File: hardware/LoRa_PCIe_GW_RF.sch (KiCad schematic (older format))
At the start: 94 parts, among them U700 NC, U800 SX1250, U801 SAW Filter, U802 SKY66423-11, U803 SAW Filter, U805 SAW Filter, U900 SX1250, Y800 TCXO

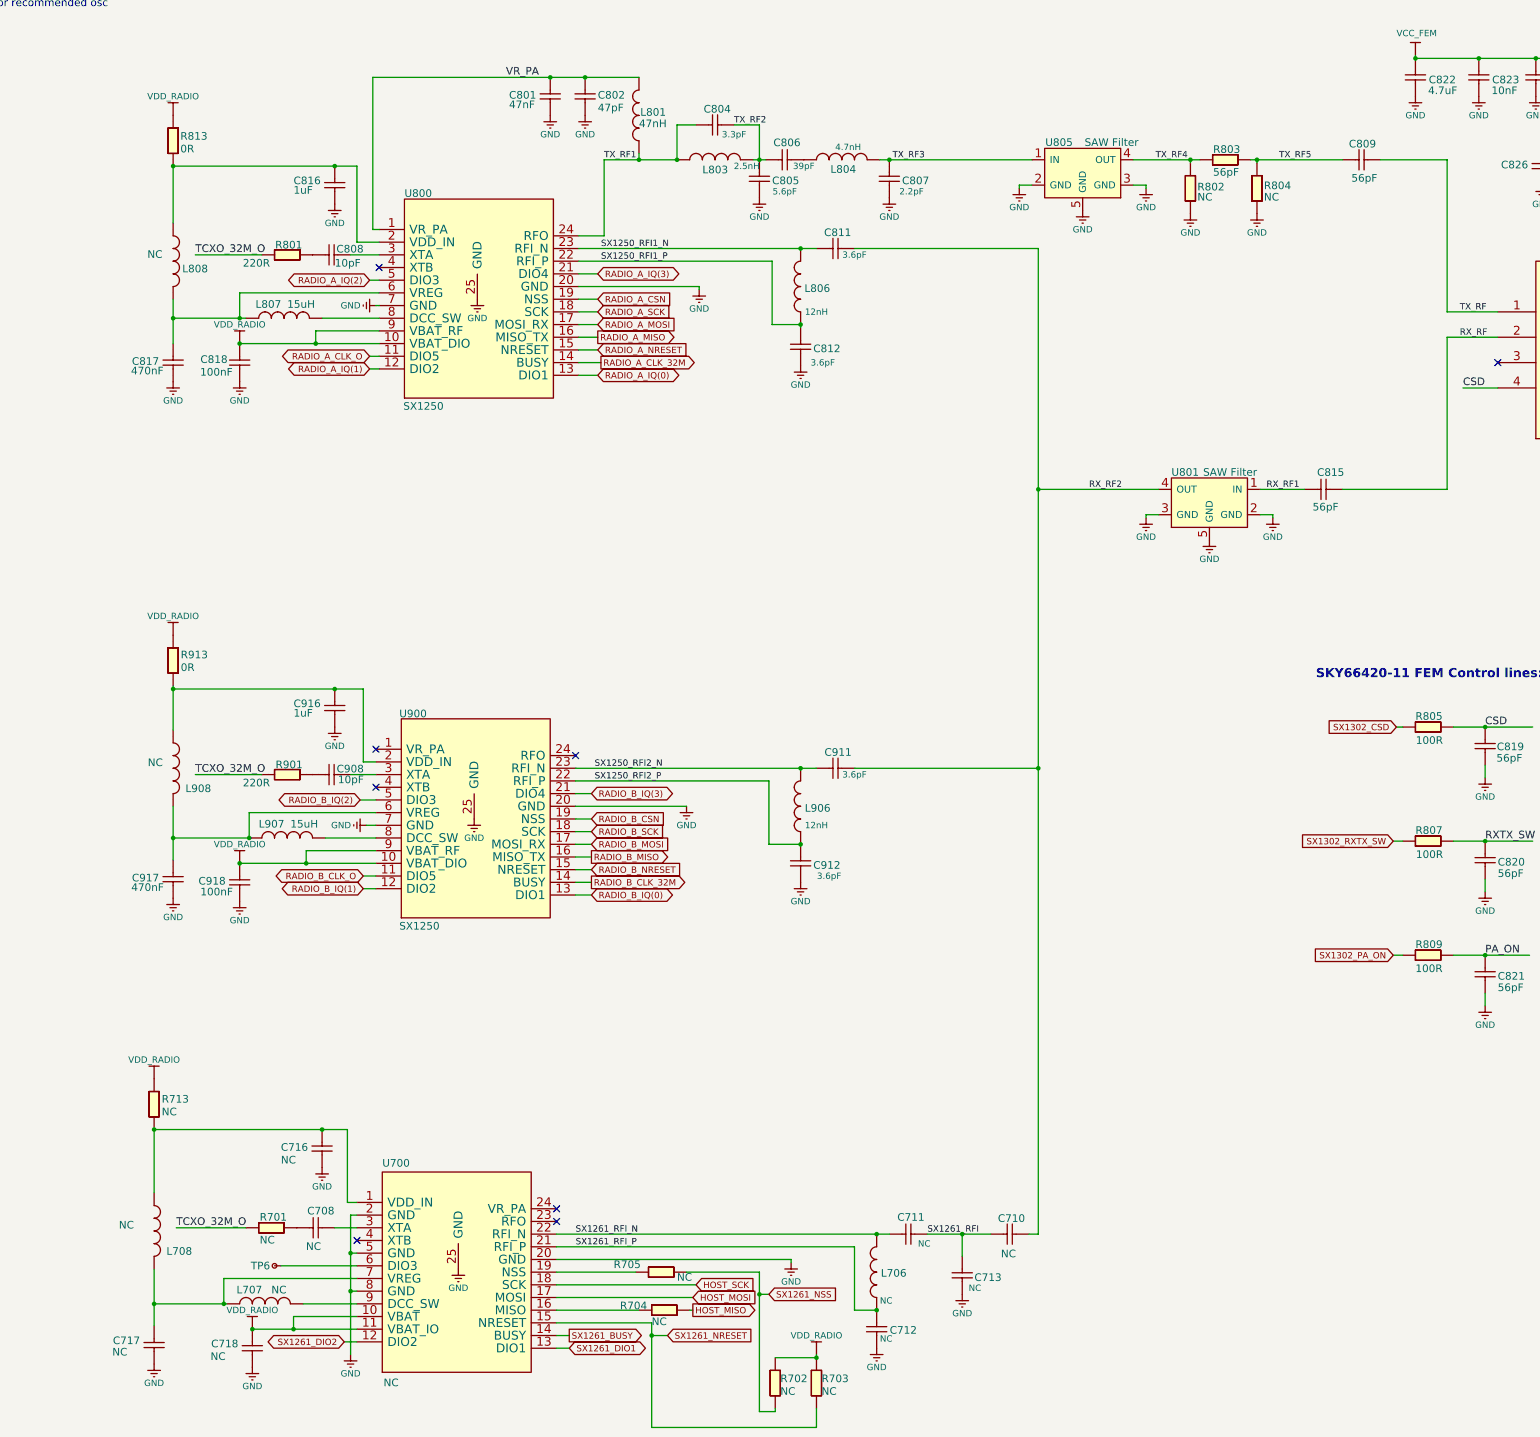
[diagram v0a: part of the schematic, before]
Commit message: Updates according to Corecell_V3 Reference design.
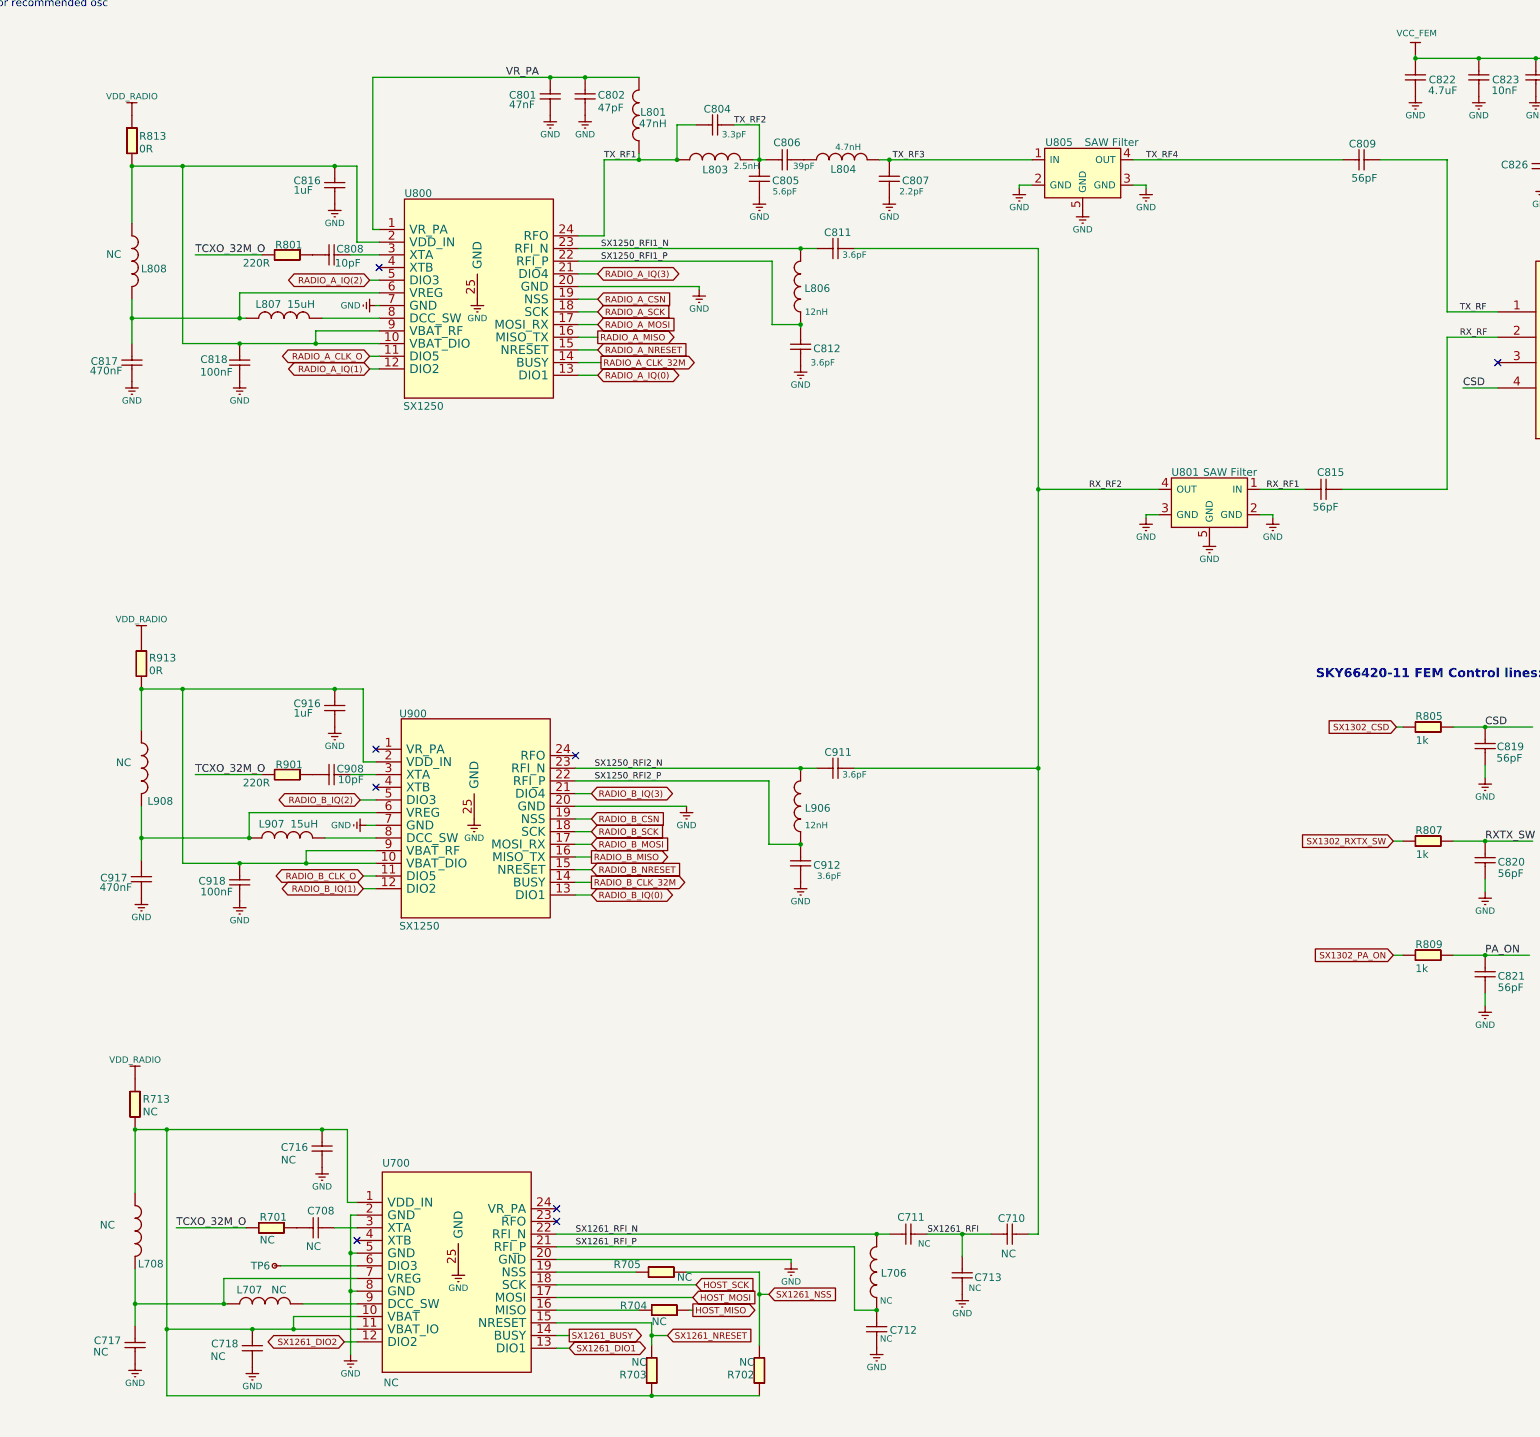
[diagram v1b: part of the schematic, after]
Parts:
- removed R802, R804: NC, LoRa_PCIe_GW:rlc_201_smd_small, symbol LoRa_PCIe_GW-rescue:Resistor-
- removed R803: 56pF, LoRa_PCIe_GW:ccer_201_smd_small, symbol LoRa_PCIe_GW-rescue:Resistor-
- C718, C818, C918: footprint LoRa_PCIe_GW:ccer_201_smd_small -> LoRa_PCIe_GW:ccer_402_smd_small; Description 0.1µF ±10% 16V Ceramic Capacitor X7S 0201 (0603 Metric) -> Multilayer ceramic capacitors X7R ±10%, 16V; Part Number GRM033C71C104KE14D -> GMD155R71C104KA11; Supplier Link https://www.digikey.com/en/products/detail/murata-electronics/GRM033C71C104KE14D/5027472 -> https://www.digikey.com/en/products/detail/murata-electronics/GMD155R71C104KA11D/10696609
- R805, R807, R809: value 100R -> 1k; Description 100 Ohms ±1% 0.05W, 1/20W Chip Resistor 0201 (0603 Metric) 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 -> 1k Ohm ±5% 0.05W, 1/20W Chip Resistor 0201 (0603 Metric) - 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; Part Number CRCW0201100R -> CRCW02011K00JNED; Price[1k] 0.037 -> 0.073; Supplier Link https://www.digikey.com/en/products/detail/vishay-dale/CRCW0201100RFKED/1967973 -> https://www.digikey.com/en/products/detail/vishay-dale/CRCW02011K00JNED/1178450
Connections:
- net TX_RF5 is gone; now on net TX_RF4: C809.1
- net VDD_RADIO: no longer C718.2, C818.2, C918.2, R702.1, R703.1, U700.10 (VBAT), U700.11 (VBAT_IO), U800.10 (VBAT_DIO), U800.9 (VBAT_RF), U900.10 (VBAT_DIO), U900.9 (VBAT_RF)
- net at C716.2, L708.2, R713.2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: now also C718.2, R702.1, R703.1, U700.10 (VBAT), U700.11 (VBAT_IO)
- net at C816.2, L808.2, R813.2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: now also C818.2, U800.10 (VBAT_DIO), U800.9 (VBAT_RF)
- net at C916.2, L908.2, R913.2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: now also C918.2, U900.10 (VBAT_DIO), U900.9 (VBAT_RF)
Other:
- moved on the sheet: C717, C817, C917, L708, L808, L908, R702, R703, R713, R813, R913

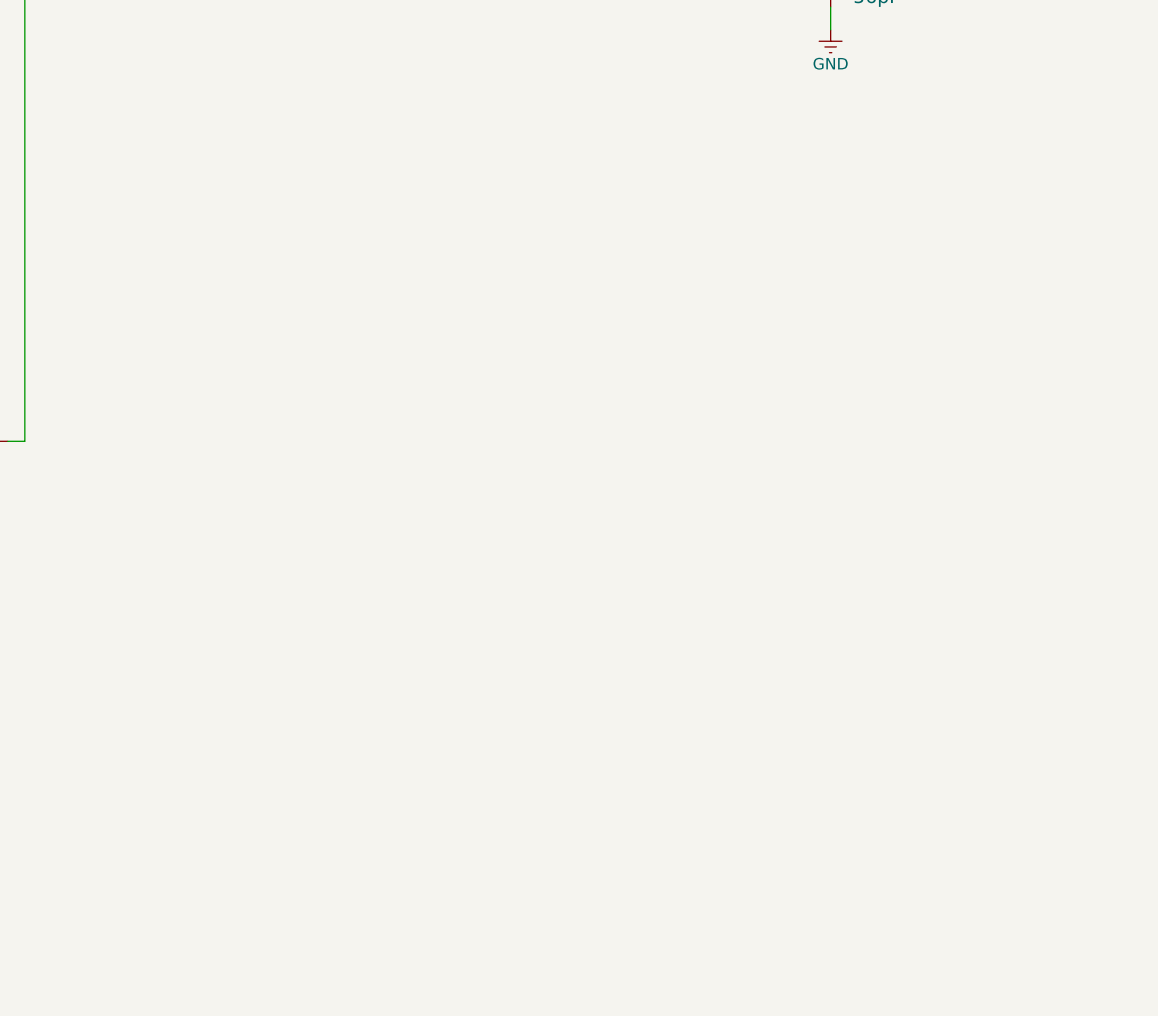
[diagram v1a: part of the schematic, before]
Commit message: Added BOM for non GNSS variants. Few part numbers corrected in design.
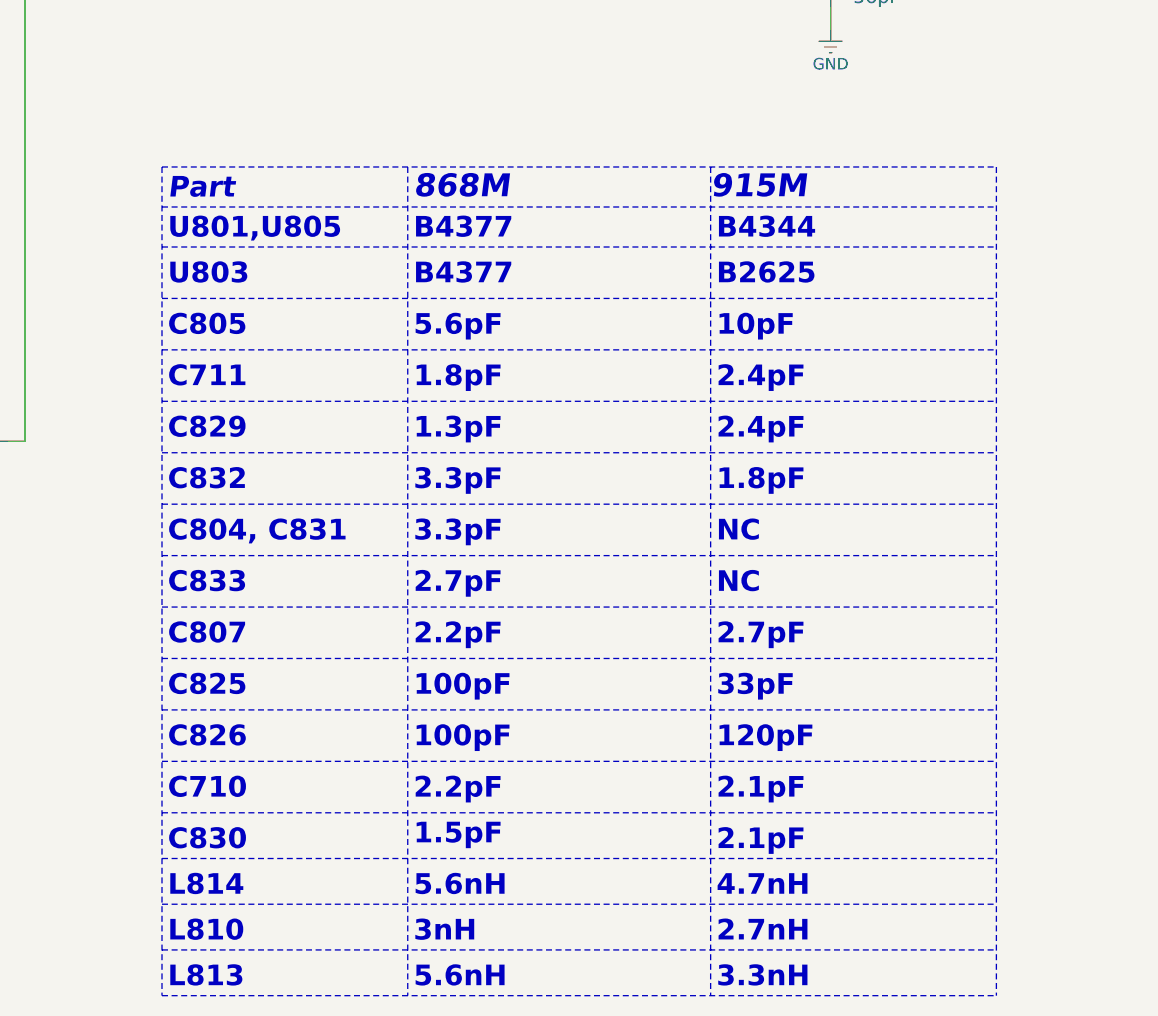
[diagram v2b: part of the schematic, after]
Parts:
- C833: Description 2.7pF ±0.25pF 25V Ceramic Capacitor C0G, NP0 0201 (0603 Met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 -> 2.7 pF ±0.1pF 50V Ceramic Capacitor C0G, NP0 0201 (0603 Met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; Part Number GJM0335C1E2R7CB01J -> GJM0335C1H2R7BB01D; Supplier Link https://www.digikey.com/en/products/detail/murata-electronics/GJM0335C1E2R7CB01J/2592574 -> https://www.digikey.com/en/products/detail/murata-electronics/GJM0335C1H2R7BB01D/9758987
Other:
- note added: "1.3pF"
- note added: "1.5pF"
- note added: "1.8pF"
- note added: "100pF"
- note added: "10pF"
- note added: "120pF"
- note added: "2.1pF"
- note added: "2.2pF"
- note added: "2.4pF"
- note added: "2.7nH"
- note added: "2.7pF"
- note added: "3.3nH"
- note added: "3.3pF"
- note added: "33pF"
- note added: "3nH"
- note added: "4.7nH"
- note added: "5.6nH"
- note added: "5.6pF"
- note added: "868M"
- note added: "915M"
- note added: "B2625"
- note added: "B4344"
- note added: "B4377"
- note added: "C710"
- note added: "C711"
- note added: "C804, C831"
- note added: "C805"
- note added: "C807"
- note added: "C825"
- note added: "C826"
- note added: "C829"
- note added: "C830"
- note added: "C832"
- note added: "C833"
- note added: "L810"
- note added: "L813"
- note added: "L814"
- note added: "NC"
- note added: "Part"
- note added: "U801,U805"
- note added: "U803"
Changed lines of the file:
@@
 F 2 "LoRa_PCIe_GW:ccer_201_smd_small" H 19500 6775 50  0001 C CNN
 F 3 "" H 19500 6775 50  0001 C CNN
-F 4 "2.7pF ±0.25pF 25V Ceramic Capacitor C0G, NP0 0201 (0603 Metric)" H 19500 6775 50  0001 C CNN "Description"
+F 4 "2.7 pF ±0.1pF 50V Ceramic Capacitor C0G, NP0 0201 (0603 Metric)" H 19500 6775 50  0001 C CNN "Description"
 F 5 "Murata" H 19500 6775 50  0001 C CNN "Manufacturer"
-F 6 "GJM0335C1E2R7CB01J" H 19500 6775 50  0001 C CNN "Part Number"
+F 6 "GJM0335C1H2R7BB01D" H 19500 6775 50  0001 C CNN "Part Number"
 F 7 "0.008" H 19500 6775 50  0001 C CNN "Price[1k]"
-F 8 "https://www.digikey.com/en/products/detail/murata-electronics/GJM0335C1E2R7CB01J/2592574" H 19500 6775 50  0001 C CNN "Supplier Link"
+F 8 "https://www.digikey.com/en/products/detail/murata-electronics/GJM0335C1H2R7BB01D/9758987" H 19500 6775 50  0001 C CNN "Supplier Link"
 	1    19500 6775
 	0    1    1    0
@@
 	8800 14550 4975 14550
 Connection ~ 4975 14025
+Wire Notes Line
+	12450 15100 16100 15100
+Wire Notes Line style solid rgb(0, 0, 0)
+	12450 12075 16100 12075
+Wire Notes Line style solid rgb(0, 0, 0)
+	12450 12250 16100 12250
+Wire Notes Line rgb(0, 0, 0)
+	12450 12425 16100 12425
+Text Notes 12475 12225 0    90   Italic 18
+Part
+Text Notes 13550 12225 0    100  Italic 20
+868M
+Text Notes 14850 12225 0    100  Italic 20
+915M
+Text Notes 12475 12400 0    90   ~ 18
+U801,U805
+Text Notes 13550 12400 0    90   ~ 18
+B4377
+Text Notes 14875 12400 0    90   ~ 18
+B4344
+Wire Notes Line
+	12450 12650 16100 12650
+Wire Notes Line
+	12450 12875 16100 12875
+Wire Notes Line
+	12450 13100 16100 13100
+Wire Notes Line
+	12450 13325 16100 13325
+Wire Notes Line
+	12450 13550 16100 13550
+Text Notes 12475 12600 0    90   ~ 18
+U803
+Text Notes 13550 12600 0    90   ~ 18
+B4377
+Text Notes 14875 12600 0    90   ~ 18
+B2625
+Text Notes 12475 12825 0    90   ~ 18
+C805
+Text Notes 13550 12825 0    90   ~ 18
+5.6pF
+Text Notes 14875 12825 0    90   ~ 18
+10pF
+Text Notes 12475 13050 0    90   ~ 18
+C711
+Text Notes 13550 13050 0    90   ~ 18
+1.8pF
+Text Notes 14875 13050 0    90   ~ 18
+2.4pF
+Text Notes 12475 13275 0    90   ~ 18
+C829
+Text Notes 13550 13275 0    90   ~ 18
+1.3pF
+Text Notes 14875 13275 0    90   ~ 18
+2.4pF
+Text Notes 12475 13500 0    90   ~ 18
+C832
+Text Notes 13550 13500 0    90   ~ 18
+3.3pF
+Text Notes 14875 13500 0    90   ~ 18
+1.8pF
+Wire Notes Line
+	12450 13775 16100 13775
+Wire Notes Line
+	12450 14000 16100 14000
+Wire Notes Line
+	12450 14225 16100 14225
+Wire Notes Line
+	12450 14450 16100 14450
+Wire Notes Line
+	12450 14675 16100 14675
+Wire Notes Line
+	12450 14900 16100 14900
+Text Notes 12475 13725 0    90   ~ 18
+C804, C831
+Text Notes 13550 13725 0    90   ~ 18
+3.3pF
+Text Notes 14875 13725 0    90   ~ 18
+NC
+Text Notes 12475 13950 0    90   ~ 18
+C833
+Text Notes 13550 13950 0    90   ~ 18
+2.7pF
+Text Notes 14875 13950 0    90   ~ 18
+NC
+Text Notes 12475 14175 0    90   ~ 18
+C807
+Text Notes 13550 14175 0    90   ~ 18
+2.2pF
+Text Notes 14875 14175 0    90   ~ 18
+2.7pF
+Text Notes 12475 14400 0    90   ~ 18
+C825
+Text Notes 13550 14400 0    90   ~ 18
+100pF
+Text Notes 14875 14400 0    90   ~ 18
+33pF
+Text Notes 12475 14625 0    90   ~ 18
+C826
+Text Notes 13550 14625 0    90   ~ 18
+100pF
+Text Notes 14875 14625 0    90   ~ 18
+120pF
+Text Notes 12475 14850 0    90   ~ 18
+C710
+Text Notes 13550 14850 0    90   ~ 18
+2.2pF
+Text Notes 14875 14850 0    90   ~ 18
+2.1pF
+Text Notes 12475 15075 0    90   ~ 18
+C830
+Text Notes 13550 15050 0    90   ~ 18
+1.5pF
+Text Notes 14875 15075 0    90   ~ 18
+2.1pF
+Wire Notes Line
+	12450 15300 16100 15300
+Wire Notes Line
+	12450 15500 16100 15500
+Wire Notes Line style solid rgb(0, 0, 0)
+	12450 15700 16100 15700
+Wire Notes Line style solid rgb(0, 0, 0)
+	12450 12075 12450 15700
+Wire Notes Line style solid rgb(0, 0, 0)
+	16100 12075 16100 15700
+Wire Notes Line
+	13525 12075 13525 15700
+Wire Notes Line
+	14850 12075 14850 15700
+Text Notes 12475 15275 0    90   ~ 18
+L814
+Text Notes 13550 15275 0    90   ~ 18
+5.6nH
+Text Notes 14875 15275 0    90   ~ 18
+4.7nH
+Text Notes 12475 15475 0    90   ~ 18
+L810
+Text Notes 13550 15475 0    90   ~ 18
+3nH
+Text Notes 14875 15475 0    90   ~ 18
+2.7nH
+Text Notes 12475 15675 0    90   ~ 18
+L813
+Text Notes 13550 15675 0    90   ~ 18
+5.6nH
+Text Notes 14875 15675 0    90   ~ 18
+3.3nH
 $EndSCHEMATC
